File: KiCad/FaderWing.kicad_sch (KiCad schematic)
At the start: 185 parts, among them J1 USB_C_Receptacle_USB2.0, SW1 Encoder_Switch, SW10 SW_Push, SW11 Encoder_Switch, SW12 SW_Push, SW13 SW_Push, SW14 SW_Push, SW15 SW_Push, SW16 Encoder_Switch, SW17 SW_Push, SW18 SW_Push, SW19 SW_Push, SW2 SW_Push, SW20 SW_Push, SW21 Encoder_Switch, SW22 SW_Push, SW23 SW_Push, SW24 SW_Push, SW25 SW_Push, SW3 SW_Push, SW4 SW_Push, SW5 SW_Push, SW6 Encoder_Switch, SW7 SW_Push, SW8 SW_Push, SW9 SW_Push, U1 USBLC6-2SC6, U2 STM32G473RCTx, U3 AP2161WG-7, U4 MIC5504-3.3YM5, U5 TXS0102DCU

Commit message: Update to revision 0.7
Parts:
- added A-F1, A-F2, A-F3, A-F4, A-F5, A-VDDA1, A-VSSA1, B-F1, B-F2, B-F3, B-F4, B-F5, B-VDDA1, B-VSSA1: TestPoint_Small, TestPoint:TestPoint_THTPad_D2.0mm_Drill1.0mm, symbol Connector:TestPoint_Small
- added PA10, PA3, PB0, PB1, PB2, PB9, PC10, PC11, PC12, PC13, PC14, PC15, PC5, PD2, PF0, PF1: TestPoint_Small, TestPoint:TestPoint_Pad_D1.0mm, symbol Connector:TestPoint_Small
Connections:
- net Fader1: now also A-F1.1, B-F1.1
- net Fader2: now also A-F2.1, B-F2.1
- net Fader3: now also A-F3.1, B-F3.1
- net Fader4: now also A-F4.1, B-F4.1
- net Fader5: now also A-F5.1, B-F5.1
- net GND: now also A-VSSA1.1, B-VSSA1.1
- net VDD: now also A-VDDA1.1, B-VDDA1.1
- net at U2.17 (PA3): now also PA3.1
- net at U2.2 (PC13): now also PC13.1
- net at U2.23 (PC5): now also PC5.1
- net at U2.24 (PB0): now also PB0.1
- net at U2.25 (PB1): now also PB1.1
- net at U2.26 (PB2): now also PB2.1
- net at U2.3 (PC14): now also PC14.1
- net at U2.4 (PC15): now also PC15.1
- net at U2.44 (PA10): now also PA10.1
- net at U2.5 (PF0): now also PF0.1
- net at U2.52 (PC10): now also PC10.1
- net at U2.53 (PC11): now also PC11.1
- net at U2.54 (PC12): now also PC12.1
- net at U2.55 (PD2): now also PD2.1
- net at U2.6 (PF1): now also PF1.1
- net at U2.62 (PB9): now also PB9.1
- no-connect marks 5 -> 6
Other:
- moved on the sheet: TP7

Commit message: Update Revision 0.8
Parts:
- added R5: 10k, Resistor_SMD:R_0603_1608Metric, symbol Device:R_Small
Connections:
- net BOOT 0: now also R5.2
- net Encoder3A: now also U2.60 (PB7); no longer U2.59 (PB6)
- net Encoder3B: now also U2.59 (PB6); no longer U2.60 (PB7)
- net Fader1: no longer B-F1.1, RV1.2
- net Fader2: no longer B-F2.1, RV2.2
- net Fader3: no longer B-F3.1, RV3.2
- net Fader4: no longer B-F4.1, RV4.2
- net Fader5: no longer B-F5.1, RV5.2
- net GND: now also R5.1; no longer B-VSSA1.1, RV1.3, RV2.3, RV3.3, RV4.3, RV5.3
- net VDD: no longer B-VDDA1.1, RV1.1, RV2.1, RV3.1, RV4.1, RV5.1
- new net Fader1-sat: B-F1.1, RV1.2
- new net Fader2-sat: B-F2.1, RV2.2
- new net Fader3-sat: B-F3.1, RV3.2
- new net Fader4-sat: B-F4.1, RV4.2
- new net Fader5-sat: B-F5.1, RV5.2
- new net Faders-GND: B-VSSA1.1, RV1.3, RV2.3, RV3.3, RV4.3, RV5.3
- new net Faders-VREF: B-VDDA1.1, RV1.1, RV2.1, RV3.1, RV4.1, RV5.1
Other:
- moved on the sheet: B-F1, B-F2, B-F3, B-F4, B-F5, C14, C19, C20, C21, C58, C59, C70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

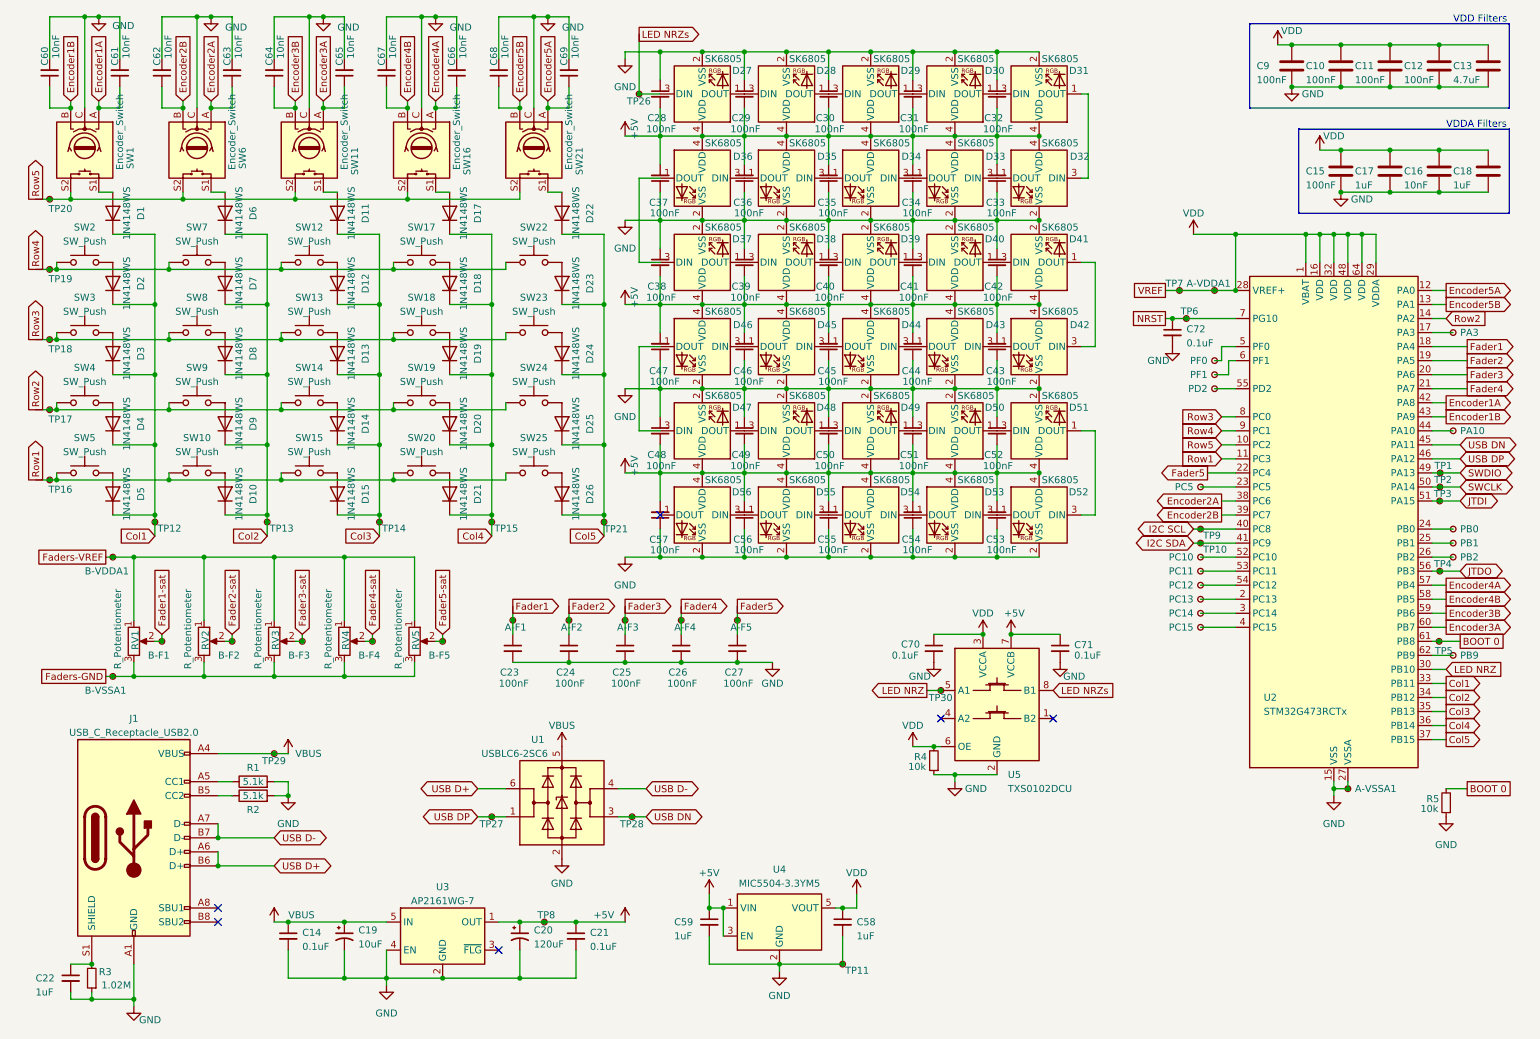
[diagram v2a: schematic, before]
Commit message: Update to V1.0
This is what I would consider as ready for fabrication

+ Power LEDs
~ Revised SK6805-EC15 footprints
+ (removeable) Series NZR protection 500Ohm resistor
~ Moved USB port and PSU to the left to shorten the USB traces
~ Update project to KiCad 8
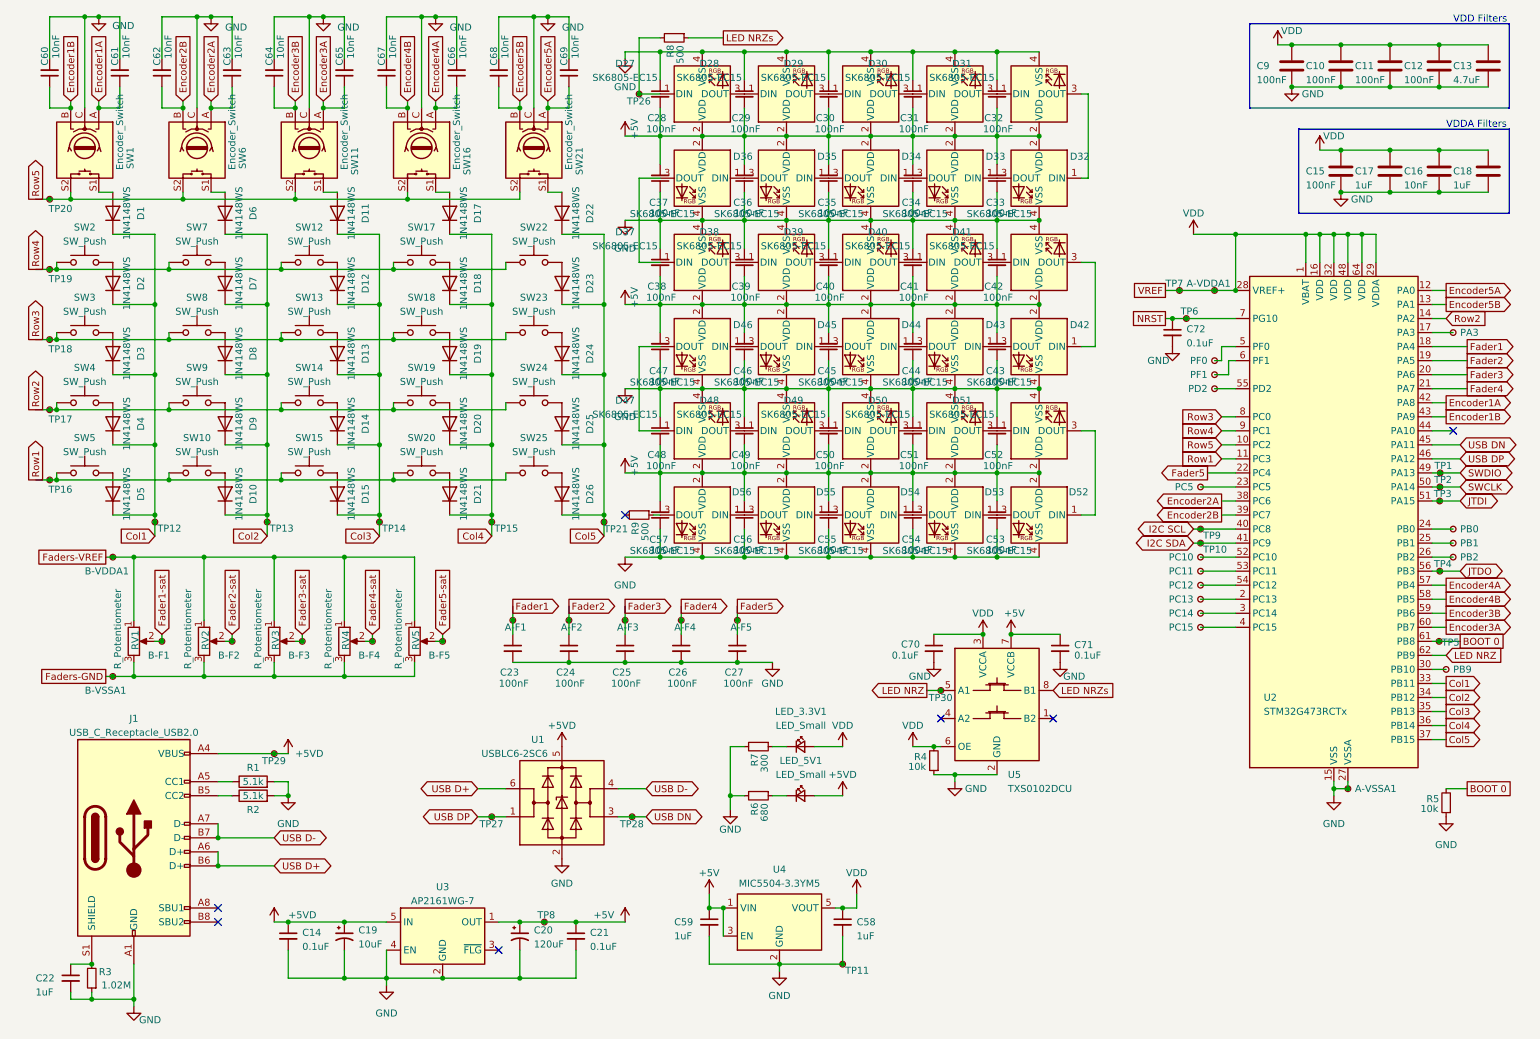
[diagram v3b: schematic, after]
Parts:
- removed PA10: TestPoint_Small, TestPoint:TestPoint_Pad_D1.0mm, symbol Connector:TestPoint_Small
- added LED_3.3V1, LED_5V1: LED_Small, LED_SMD:LED_1206_3216Metric, symbol Device:LED_Small
- added R6: 680, Resistor_SMD:R_0603_1608Metric, symbol Device:R_Small
- added R7: 300, Resistor_SMD:R_0603_1608Metric, symbol Device:R_Small
- added R8, R9: 500, Resistor_SMD:R_0603_1608Metric, symbol Device:R_Small
- D27, D28, D29, D30, D31, D32, D33, D34, D35, D36, D37, D38, D39, D40, D41, D42, D43, D44, D45, D46, D47, D48, D49, D50, D51, D52, D53, D54, D55, D56: value SK6805 -> SK6805-EC15; footprint LED_SMD:LED_SK6812_EC15_1.5x1.5mm -> Custom:LED_SK6805_EC15_1.5x1.5mm; symbol LED:SK6805 -> Custom:SK6805-EC15
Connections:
- net +5V: now also D27.2 (VDD), D28.2 (VDD), D29.2 (VDD), D30.2 (VDD), D31.2 (VDD), D32.2 (VDD), D33.2 (VDD), D34.2 (VDD), D35.2 (VDD), D36.2 (VDD), D37.2 (VDD), D38.2 (VDD), D39.2 (VDD), D40.2 (VDD), D41.2 (VDD), D42.2 (VDD), D43.2 (VDD), D44.2 (VDD), D45.2 (VDD), D46.2 (VDD), D47.2 (VDD), D48.2 (VDD), D49.2 (VDD), D50.2 (VDD), D51.2 (VDD), D52.2 (VDD), D53.2 (VDD), D54.2 (VDD), D55.2 (VDD), D56.2 (VDD); no longer D27.4 (VDD), D28.4 (VDD), D29.4 (VDD), D30.4 (VDD), D31.4 (VDD), D32.4 (VDD), D33.4 (VDD), D34.4 (VDD), D35.4 (VDD), D36.4 (VDD), D37.4 (VDD), D38.4 (VDD), D39.4 (VDD), D40.4 (VDD), D41.4 (VDD), D42.4 (VDD), D43.4 (VDD), D44.4 (VDD), D45.4 (VDD), D46.4 (VDD), D47.4 (VDD), D48.4 (VDD), D49.4 (VDD), D50.4 (VDD), D51.4 (VDD), D52.4 (VDD), D53.4 (VDD), D54.4 (VDD), D55.4 (VDD), D56.4 (VDD)
- net +5VD: now also LED_5V1.2 (A)
- net GND: now also D27.4 (VSS), D28.4 (VSS), D29.4 (VSS), D30.4 (VSS), D31.4 (VSS), D32.4 (VSS), D33.4 (VSS), D34.4 (VSS), D35.4 (VSS), D36.4 (VSS), D37.4 (VSS), D38.4 (VSS), D39.4 (VSS), D40.4 (VSS), D41.4 (VSS), D42.4 (VSS), D43.4 (VSS), D44.4 (VSS), D45.4 (VSS), D46.4 (VSS), D47.4 (VSS), D48.4 (VSS), D49.4 (VSS), D50.4 (VSS), D51.4 (VSS), D52.4 (VSS), D53.4 (VSS), D54.4 (VSS), D55.4 (VSS), D56.4 (VSS), R6.2, R7.2; no longer D27.2 (VSS), D28.2 (VSS), D29.2 (VSS), D30.2 (VSS), D31.2 (VSS), D32.2 (VSS), D33.2 (VSS), D34.2 (VSS), D35.2 (VSS), D36.2 (VSS), D37.2 (VSS), D38.2 (VSS), D39.2 (VSS), D40.2 (VSS), D41.2 (VSS), D42.2 (VSS), D43.2 (VSS), D44.2 (VSS), D45.2 (VSS), D46.2 (VSS), D47.2 (VSS), D48.2 (VSS), D49.2 (VSS), D50.2 (VSS), D51.2 (VSS), D52.2 (VSS), D53.2 (VSS), D54.2 (VSS), D55.2 (VSS), D56.2 (VSS)
- net LED NRZ: now also U2.62 (PB9); no longer U2.30 (PB10)
- net LED NRZs: now also R8.1; no longer D27.3 (DIN), TP26.1
- net VDD: now also LED_3.3V1.2 (A)
- net at D39.1 (DIN): now also D38.3 (DOUT); no longer D40.3 (DIN)
- net at D39.3 (DOUT): now also D40.1 (DIN); no longer D38.1 (DOUT)
- net at D49.1 (DIN): now also D48.3 (DOUT); no longer D50.3 (DIN)
- net at D49.3 (DOUT): now also D50.1 (DIN); no longer D48.1 (DOUT)
- net at D55.1 (DIN): now also D54.3 (DOUT); no longer D56.3 (DIN)
- net at D55.3 (DOUT): now also D56.1 (DIN); no longer D54.1 (DOUT)
- net at D43.1 (DIN): now also D42.3 (DOUT); no longer D44.3 (DIN)
- net at D43.3 (DOUT): now also D44.1 (DIN); no longer D42.1 (DOUT)
- net at D30.1 (DIN): now also D29.3 (DOUT); no longer D31.3 (DIN)
- net at D30.3 (DOUT): now also D31.1 (DIN); no longer D29.1 (DOUT)
- net at D41.1 (DIN): now also D40.3 (DOUT); no longer D42.3 (DIN)
- net at D47.1 (DIN): now also D46.3 (DOUT); no longer D48.3 (DIN)
- net at D36.1 (DIN): now also D35.3 (DOUT); no longer D37.3 (DIN)
- net at D36.3 (DOUT): now also D37.1 (DIN); no longer D35.1 (DOUT)
- net at D51.3 (DOUT): now also D52.1 (DIN); no longer D50.1 (DOUT)
- net at PB9.1: now also U2.30 (PB10); no longer U2.62 (PB9)
- net at D32.3 (DOUT): now also D33.1 (DIN); no longer D31.1 (DOUT)
- net at D27.1 (DIN): now also TP26.1, R8.2; no longer D28.3 (DIN)
- net at D45.3 (DOUT): now also D46.1 (DIN); no longer D44.1 (DOUT)
- net at D41.3 (DOUT): now also D42.1 (DIN); no longer D40.1 (DOUT)
- net at D32.1 (DIN): now also D31.3 (DOUT); no longer D33.3 (DIN)
- net at D53.3 (DOUT): now also D54.1 (DIN); no longer D52.1 (DOUT)
- net at D51.1 (DIN): now also D50.3 (DOUT); no longer D52.3 (DIN)
- net at D28.1 (DIN): now also D27.3 (DOUT); no longer D29.3 (DIN)
- net at D53.1 (DIN): now also D52.3 (DOUT); no longer D54.3 (DIN)
- net at D34.1 (DIN): now also D33.3 (DOUT); no longer D35.3 (DIN)
- net at D34.3 (DOUT): now also D35.1 (DIN); no longer D33.1 (DOUT)
- net at D47.3 (DOUT): now also D48.1 (DIN); no longer D46.1 (DOUT)
- net at D45.1 (DIN): now also D44.3 (DOUT); no longer D46.3 (DIN)
- new net: D56.3 (DOUT), R9.1
- new net: LED_5V1.1 (K), R6.1
- new net: LED_3.3V1.1 (K), R7.1
- new net: D28.3 (DOUT), D29.1 (DIN)
- new net: D37.3 (DOUT), D38.1 (DIN)
- no-connect marks 6 -> 7
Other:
- moved on the sheet: PB9

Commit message: Improve components routing
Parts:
- renumbered TP30 to 3vNz1, TP26 to 5vNz1, LED_3.3V1 to LED-3V1, LED_5V1 to LED-5V1, PB9 to PB10
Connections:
- net LED NRZs: now also 5vNz1.1
- net at D27.1 (DIN), R8.2: no longer 5vNz1.1
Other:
- moved on the sheet: 5vNz1
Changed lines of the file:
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@@
 	)
 	(junction
-		(at 125.73 27.94)
-		(diameter 0)
-		(color 0 0 0 0)
-	)
-	(junction
 		(at 129.54 96.52)
 		(diameter 0)
@@
 	)
 	(junction
+		(at 137.16 17.78)
+		(diameter 0)
+		(color 0 0 0 0)
+	)
+	(junction
 		(at 99.06 105.41)
 		(diameter 0)
@@
 	(wire
 		(pts
-			(xy 140.97 17.78) (xy 134.62 17.78)
+			(xy 140.97 17.78) (xy 137.16 17.78)
 		)
 		(stroke
@@
 	(wire
 		(pts
-			(xy 165.1 172.72) (xy 165.1 175.26)
+			(xy 182.88 151.13) (xy 190.5 151.13)
 		)
 		(stroke
@@
 	(wire
 		(pts
-			(xy 182.88 151.13) (xy 190.5 151.13)
+			(xy 125.73 17.78) (xy 125.73 27.94)
 		)
 		(stroke
@@
 	(wire
 		(pts
-			(xy 125.73 17.78) (xy 125.73 27.94)
+			(xy 71.12 66.04) (xy 78.74 66.04)
 		)
 		(stroke
@@
 	(wire
 		(pts
-			(xy 71.12 66.04) (xy 78.74 66.04)
+			(xy 233.68 53.34) (xy 246.38 53.34)
 		)
 		(stroke
@@
 	(wire
 		(pts
-			(xy 233.68 53.34) (xy 246.38 53.34)
+			(xy 165.1 172.72) (xy 165.1 175.26)
 		)
 		(stroke
@@
 	(wire
 		(pts
+			(xy 137.16 17.78) (xy 134.62 17.78)
+		)
+		(stroke
+			(width 0)
+			(type default)
+		)
+	)
+	(wire
+		(pts
 			(xy 111.76 66.04) (xy 119.38 66.04)
 		)
@@
 		(on_board yes)
 		(dnp no)
-		(property "Reference" "TP30"
+		(property "Reference" "3vNz1"
 			(at 178.1271 137.2046 0)
 			(effects
@@
 			(project "FaderWing"
 				(path "/2c43a361-34f1-4ae2-be8b-387d563946da"
-					(reference "TP30")
+					(reference "3vNz1")
 					(unit 1)
 				)
@@
 		(dnp no)
 		(fields_autoplaced yes)
-		(property "Reference" "LED_5V1"
+		(property "Reference" "LED-5V1"
 			(at 155.0035 148.59 0)
 			(effects
@@
 			(project "FaderWing"
 				(path "/2c43a361-34f1-4ae2-be8b-387d563946da"
-					(reference "LED_5V1")
+					(reference "LED-5V1")
 					(unit 1)
 				)
@@
 		(dnp no)
 		(fields_autoplaced yes)
-		(property "Reference" "LED_3.3V1"
+		(property "Reference" "LED-3V1"
 			(at 155.0035 139.7 0)
 			(effects
@@
 			(project "FaderWing"
 				(path "/2c43a361-34f1-4ae2-be8b-387d563946da"
-					(reference "LED_3.3V1")
+					(reference "LED-3V1")
 					(unit 1)
 				)
@@
 	(symbol
 		(lib_id "Connector:TestPoint_Small")
-		(at 125.73 27.94 0)
+		(at 137.16 17.78 0)
 		(unit 1)
 		(exclude_from_sim no)
@@
 		(on_board yes)
 		(dnp no)
-		(property "Reference" "TP26"
-			(at 123.5171 29.2546 0)
+		(property "Reference" "5vNz1"
+			(at 134.62 16.256 0)
 			(effects
 				(font
@@
 		)
 		(property "Value" "TestPoint_Small"
-			(at 127 29.845 0)
+			(at 138.43 19.685 0)
 			(effects
 				(font
@@
 		)
 		(property "Footprint" "TestPoint:TestPoint_Pad_D1.0mm"
-			(at 130.81 27.94 0)
+			(at 142.24 17.78 0)
 			(effects
 				(font
@@
 		)
 		(property "Datasheet" "~"
-			(at 130.81 27.94 0)
+			(at 142.24 17.78 0)
 			(effects
 				(font
@@
 		)
 		(property "Description" ""
-			(at 125.73 27.94 0)
+			(at 137.16 17.78 0)
 			(effects
 				(font
@@
 			(project "FaderWing"
 				(path "/2c43a361-34f1-4ae2-be8b-387d563946da"
-					(reference "TP26")
+					(reference "5vNz1")
 					(unit 1)
 				)
@@
 		(on_board yes)
 		(dnp no)
-		(property "Reference" "PB9"
+		(property "Reference" "PB10"
 			(at 273.05 132.08 0)
 			(effects
@@
 			(project "FaderWing"
 				(path "/2c43a361-34f1-4ae2-be8b-387d563946da"
-					(reference "PB9")
+					(reference "PB10")
 					(unit 1)
 				)

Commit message: Update components to use less dumb packages
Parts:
- A-VDDA1, A-VSSA1, PA3, PB0, PB1, PB10, PB2, PC10, PC11, PC12, PC13, PC14, PC15, PC5, PD2, PF0, PF1, RV1, RV2, RV3, RV4, RV5, SW1, SW10, SW11, SW12, SW13, SW14, SW15, SW16, SW17, SW18, SW19, SW2, SW20, SW21, SW22, SW23, SW24, SW25, SW3, SW4, SW5, SW6, SW7, SW8, SW9, TP1, TP10, TP11, TP12, TP13, TP14, TP15, TP16, TP17, TP18, TP19, TP2, TP21, TP27, TP28, TP29, TP3, TP4, TP5, TP6, TP7, TP8, TP9: now left out of the parts list
- C16, C60, C61, C62, C63, C64, C65, C66, C67, C68, C69: footprint Capacitor_SMD:C_0603_1608Metric -> Capacitor_SMD:C_0402_1005Metric
- C19: footprint Capacitor_Tantalum_SMD:CP_EIA-3216-10_Kemet-I -> Capacitor_Tantalum_SMD:CP_EIA-3216-18_Kemet-A
- J1: footprint Connector_USB:USB_C_Receptacle_Palconn_UTC16-G -> Connector_USB:USB_C_Receptacle_GCT_USB4105-xx-A_16P_TopMnt_Horizontal
- R3: value 1.02M -> 1M
- R8, R9: value 500 -> 510
- TPNZ1: renamed from 3vNz1; now left out of the parts list
- TPNZ2: renamed from 5vNz1; now left out of the parts list
- renumbered LED-3V1 to LD1, LED-5V1 to LD2

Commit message: Fix 5v LED resistor
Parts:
- R6: value 680 -> 1.2k
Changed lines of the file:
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@@
 			)
 		)
-		(property "Value" "680"
+		(property "Value" "1.2k"
 			(at 148.4094 157.9655 0)
 			(effects

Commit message: Remove cutout in the middle of the board to reduce costs (custom panelling)
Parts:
- R7: value 300 -> 350
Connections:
- net Fader1-sat is gone; now on net Fader1: B-F1.1, RV1.2
- net Fader2-sat is gone; now on net Fader2: B-F2.1, RV2.2
- net Fader3-sat is gone; now on net Fader3: B-F3.1, RV3.2
- net Fader4-sat is gone; now on net Fader4: B-F4.1, RV4.2
- net Fader5-sat is gone; now on net Fader5: B-F5.1, RV5.2
- net Faders-GND is gone; now on net GND: B-VSSA1.1, RV1.3, RV2.3, RV3.3, RV4.3, RV5.3
- net Faders-VREF is gone; now on net VDD: B-VDDA1.1, RV1.1, RV2.1, RV3.1, RV4.1, RV5.1
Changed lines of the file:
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@@
 		)
 	)
-	(global_label "Fader1-sat"
+	(global_label "Fader1"
 		(shape input)
 		(at 39.37 125.73 90)
@@
 		)
 		(property "Intersheetrefs" "${INTERSHEET_REFS}"
-			(at 39.37 111.8781 90)
+			(at 39.37 116.2739 90)
 			(effects
 				(font
@@
 		)
 	)
-	(global_label "Faders-GND"
+	(global_label "GND"
 		(shape passive)
 		(at 29.21 133.35 180)
@@
 		)
 		(property "Intersheetrefs" "${INTERSHEET_REFS}"
-			(at 15.6831 133.35 0)
+			(at 23.4656 133.35 0)
 			(effects
 				(font
@@
 		)
 	)
-	(global_label "Faders-VREF"
+	(global_label "VREF"
 		(shape passive)
 		(at 29.21 111.76 180)
@@
 		)
 		(property "Intersheetrefs" "${INTERSHEET_REFS}"
-			(at 14.9574 111.76 0)
+			(at 22.7399 111.76 0)
 			(effects
 				(font
@@
 		)
 	)
-	(global_label "Fader4-sat"
+	(global_label "Fader4"
 		(shape input)
 		(at 77.47 125.73 90)
@@
 		)
 		(property "Intersheetrefs" "${INTERSHEET_REFS}"
-			(at 77.47 111.8781 90)
+			(at 77.47 116.2739 90)
 			(effects
 				(font
@@
 		)
 	)
-	(global_label "Fader2-sat"
+	(global_label "Fader2"
 		(shape input)
 		(at 52.07 125.73 90)
@@
 		)
 		(property "Intersheetrefs" "${INTERSHEET_REFS}"
-			(at 52.07 111.8781 90)
+			(at 52.07 116.2739 90)
 			(effects
 				(font
@@
 		)
 	)
-	(global_label "Fader3-sat"
+	(global_label "Fader3"
 		(shape input)
 		(at 64.77 125.73 90)
@@
 		)
 		(property "Intersheetrefs" "${INTERSHEET_REFS}"
-			(at 64.77 111.8781 90)
+			(at 64.77 116.2739 90)
 			(effects
 				(font
@@
 		)
 	)
-	(global_label "Fader5-sat"
+	(global_label "Fader5"
 		(shape input)
 		(at 90.17 125.73 90)
@@
 		)
 		(property "Intersheetrefs" "${INTERSHEET_REFS}"
-			(at 90.17 111.8781 90)
+			(at 90.17 116.2739 90)
 			(effects
 				(font
@@
 			)
 		)
-		(property "Value" "300"
+		(property "Value" "350"
 			(at 148.4094 149.0755 0)
 			(effects
